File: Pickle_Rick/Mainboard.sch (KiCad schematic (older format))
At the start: 82 parts, among them J10 Conn_01x02_Male, J12 Conn_01x02_Male, J2 8P8C_LED, J3 Micro_SD_Card_Det, J9 Conn_01x02_Male, Q1 MMDT2222A, Q3 PMV20ENR, U1 CP2102N-A01-GQFN24, U2 SN65HVD230, U3 ESP32-WROOM-32D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

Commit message: updated optocoupler, usb kinda weird atm ¯\_(ツ)_/¯
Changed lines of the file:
@@
 $EndComp
 $Sheet
-S 1050 3800 550  800
+S 850  3800 750  750
 U 602F075A
 F0 "usb-c" 50
@@
 F2 "usb_D+" I R 1600 4100 50
 F3 "usb_D-" I R 1600 4250 50
-F4 "usb_ID" I R 1600 4400 50
-F5 "usb_VBUS" I R 1600 3950 50
+F4 "usb_VBUS" I R 1600 3950 50
+F5 "usb_DETONATOR" I R 1600 4400 50
 $EndSheet
 Wire Wire Line

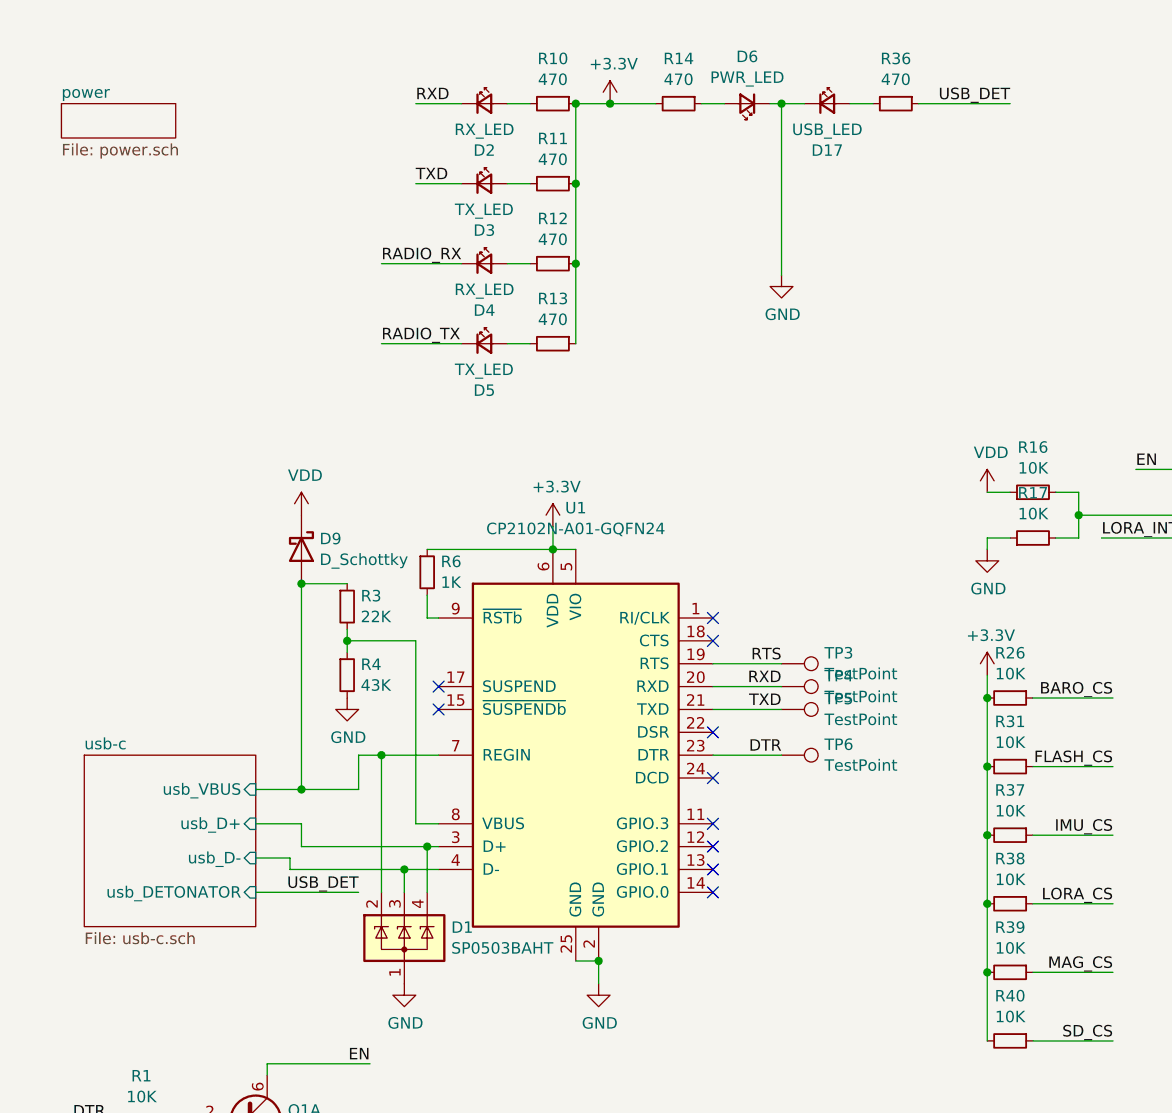
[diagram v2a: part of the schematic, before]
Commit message: fixed led circuit/made sure cc pins are independent
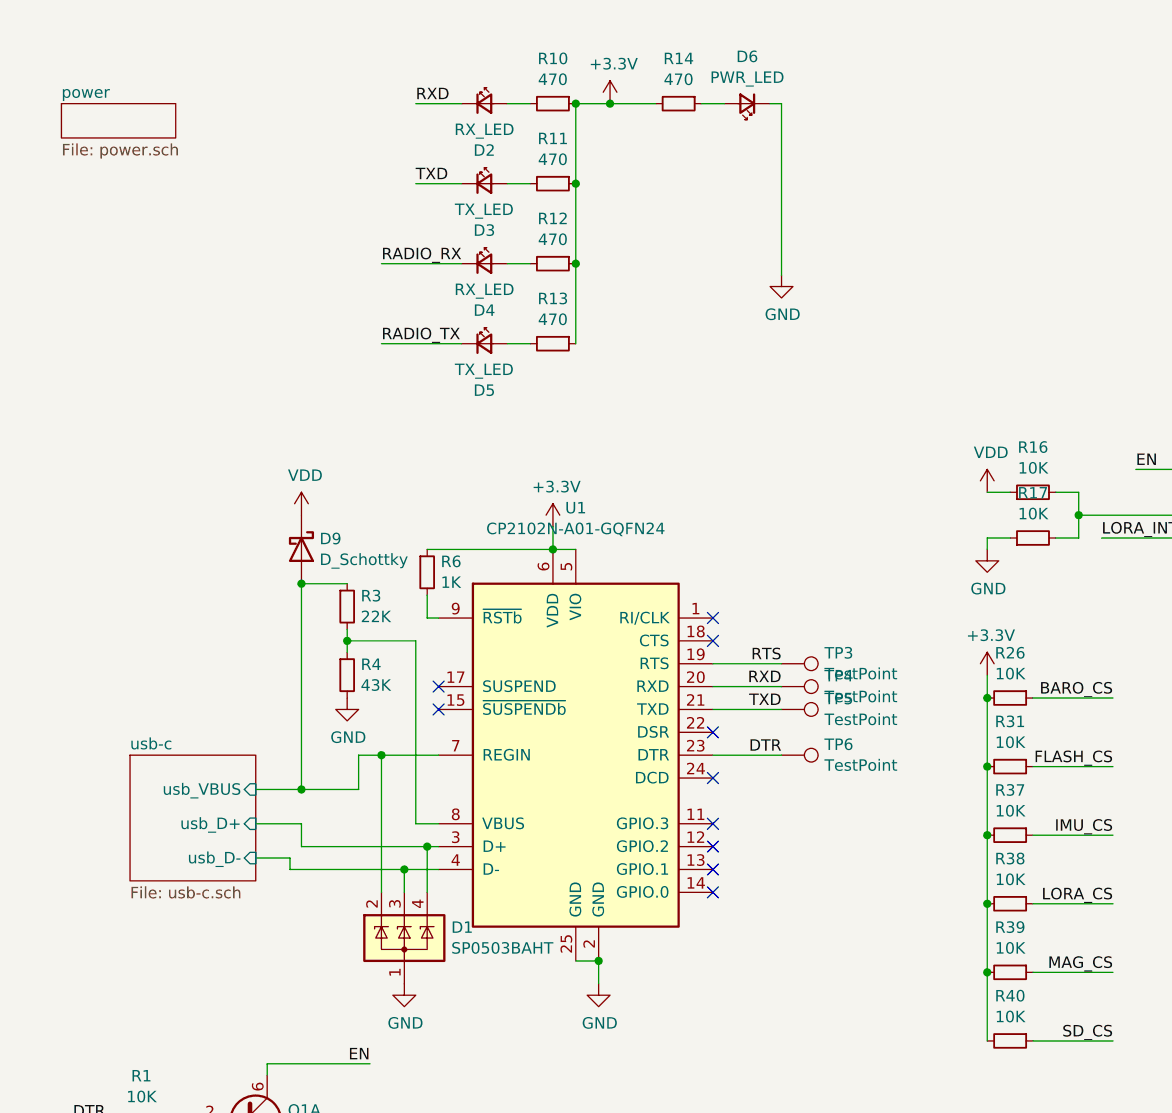
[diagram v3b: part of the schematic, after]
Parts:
- removed D17: USB_LED, LED_SMD:LED_0603_1608Metric_Castellated, symbol Device:LED_Small
- removed R36: 470, Resistor_SMD:R_0603_1608Metric, symbol Device:R_Small
- JP2: footprint iclr-hw:XBEE -> iclr:XBEE
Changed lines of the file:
@@
 SD_CS
-$Comp
-L Sensor_Pressure:MS5607-02BA U5
-U 1 1 5DAF7991
-P 10300 4600
-F 0 "U5" H 10630 4646 50  0000 L CNN
-F 1 "MS5607-02BA" H 10630 4555 50  0000 L CNN
-F 2 "Package_LGA:LGA-8_3x5mm_P1.25mm" H 10300 4600 50  0001 C CNN
-F 3 "https://www.te.com/commerce/DocumentDelivery/DDEController?Action=showdoc&DocId=Data+Sheet%7FMS5607-02BA03%7FB2%7Fpdf%7FEnglish%7FENG_DS_MS5607-02BA03_B2.pdf%7FCAT-BLPS0035" H 10300 4600 50  0001 C CNN
-	1    10300 4600
-	1    0    0    -1
-$EndComp
 $Comp
 L power:+3.3V #PWR034
@@
 F 0 "JP2" H 10350 3910 45  0000 C CNN
 F 1 "XBEE" H 10350 3826 45  0000 C CNN
-F 2 "iclr-hw:XBEE" H 10350 3750 20  0001 C CNN
+F 2 "iclr:XBEE" H 10350 3750 20  0001 C CNN
 F 3 "" H 10350 3150 50  0001 C CNN
 F 4 "XXX-00000" H 10350 3731 60  0000 C CNN "Field4"
@@
 Text Label 2150 2000 0    50   ~ 0
 RADIO_TX
-Text Label 2050 4400 2    50   ~ 0
-USB_DET
-$Comp
-L Device:LED_Small D17
-U 1 1 5DFAB0B1
-P 4100 950
-F 0 "D17" H 4100 745 50  0000 C CNN
-F 1 "USB_LED" H 4100 836 50  0000 C CNN
-F 2 "LED_SMD:LED_0603_1608Metric_Castellated" V 4100 950 50  0001 C CNN
-F 3 "~" V 4100 950 50  0001 C CNN
-	1    4100 950
-	1    0    0    -1
-$EndComp
-$Comp
-L Device:R_Small R36
-U 1 1 5DFAB0B7
-P 4400 950
-F 0 "R36" V 4204 950 50  0000 C CNN
-F 1 "470" V 4295 950 50  0000 C CNN
-F 2 "Resistor_SMD:R_0603_1608Metric" H 4400 950 50  0001 C CNN
-F 3 "~" H 4400 950 50  0001 C CNN
-	1    4400 950
-	0    1    1    0
-$EndComp
-Wire Wire Line
-	4200 950  4300 950
-Wire Wire Line
-	4000 950  3900 950
-Connection ~ 3900 950
-Wire Wire Line
-	4500 950  4900 950
-Text Label 4900 950  2    50   ~ 0
-USB_DET
 $Comp
 L Connector:Conn_01x02_Male J9
@@
 $EndComp
 $Sheet
-S 850  3800 750  750
+S 1050 3800 550  550
 U 602F075A
 F0 "usb-c" 50
@@
 F3 "usb_D-" I R 1600 4250 50
 F4 "usb_VBUS" I R 1600 3950 50
-F5 "usb_DETONATOR" I R 1600 4400 50
 $EndSheet
-Wire Wire Line
-	1600 4400 2050 4400
 Wire Wire Line
 	1800 4200 1800 4100
@@
 	-1   0    0    1
 $EndComp
+$Comp
+L Sensor_Pressure:MS5607-02BA U5
+U 1 1 5DAF7991
+P 10300 4600
+F 0 "U5" H 10630 4646 50  0000 L CNN
+F 1 "MS5607-02BA" H 10630 4555 50  0000 L CNN
+F 2 "Package_LGA:LGA-8_3x5mm_P1.25mm" H 10300 4600 50  0001 C CNN
+F 3 "https://www.te.com/commerce/DocumentDelivery/DDEController?Action=showdoc&DocId=Data+Sheet%7FMS5607-02BA03%7FB2%7Fpdf%7FEnglish%7FENG_DS_MS5607-02BA03_B2.pdf%7FCAT-BLPS0035" H 10300 4600 50  0001 C CNN
+	1    10300 4600
+	1    0    0    -1
+$EndComp
 $EndSCHEMATC

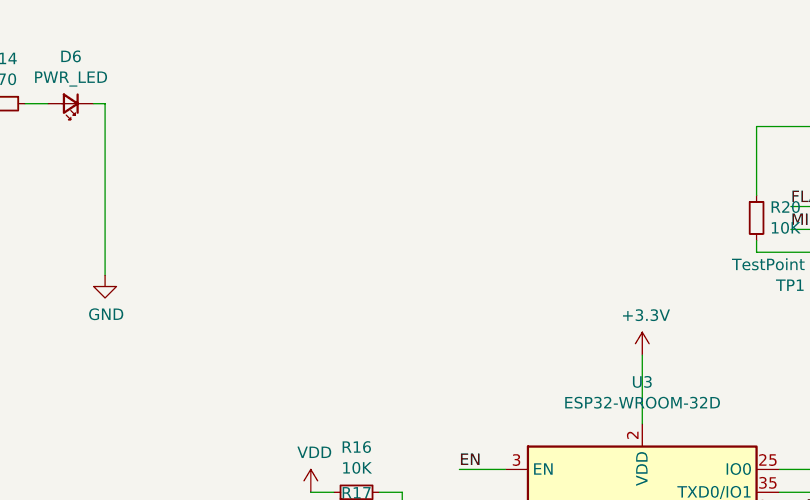
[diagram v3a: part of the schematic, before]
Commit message: might or not have added a rgb port
still need to pick usb footprint; look into smaller buzzer?
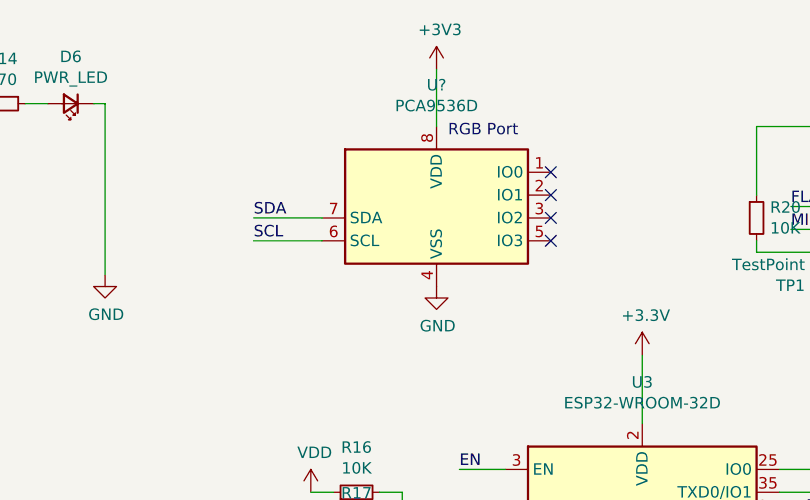
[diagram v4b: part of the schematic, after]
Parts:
- added U?: PCA9536D, Package_SO:SOIC-8_3.9x4.9mm_P1.27mm, symbol Interface_Expansion:PCA9536D
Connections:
- net +3V3: now also U?.8 (VDD)
- net GND: now also U?.4 (VSS)
- net SCL: now also U?.6 (SCL)
- net SDA: now also U?.7 (SDA)
- no-connect marks 40 -> 44
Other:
- note added: "RGB Port"
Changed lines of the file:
@@
 	1    0    0    -1
 $EndComp
+$Comp
+L Interface_Expansion:PCA9536D U?
+U 1 1 60497087
+P 5350 1350
+F 0 "U?" H 5350 1831 50  0000 C CNN
+F 1 "PCA9536D" H 5350 1740 50  0000 C CNN
+F 2 "Package_SO:SOIC-8_3.9x4.9mm_P1.27mm" H 6350 1000 50  0001 C CNN
+F 3 "http://www.nxp.com/documents/data_sheet/PCA9536.pdf" H 5150 -350 50  0001 C CNN
+	1    5350 1350
+	1    0    0    -1
+$EndComp
+$Comp
+L power:+3V3 #PWR?
+U 1 1 604BFA09
+P 5350 800
+F 0 "#PWR?" H 5350 650 50  0001 C CNN
+F 1 "+3V3" H 5365 973 50  0000 C CNN
+F 2 "" H 5350 800 50  0001 C CNN
+F 3 "" H 5350 800 50  0001 C CNN
+	1    5350 800
+	1    0    0    -1
+$EndComp
+$Comp
+L power:GND #PWR?
+U 1 1 604C1D4C
+P 5350 1750
+F 0 "#PWR?" H 5350 1500 50  0001 C CNN
+F 1 "GND" H 5355 1577 50  0000 C CNN
+F 2 "" H 5350 1750 50  0001 C CNN
+F 3 "" H 5350 1750 50  0001 C CNN
+	1    5350 1750
+	1    0    0    -1
+$EndComp
+Wire Wire Line
+	5350 800  5350 1050
+Text Notes 5400 1100 0    50   ~ 0
+RGB Port
+NoConn ~ 5850 1250
+NoConn ~ 5850 1350
+NoConn ~ 5850 1450
+NoConn ~ 5850 1550
+Wire Wire Line
+	4850 1450 4550 1450
+Wire Wire Line
+	4850 1550 4550 1550
+Text Label 4550 1450 0    50   ~ 0
+SDA
+Text Label 4550 1550 0    50   ~ 0
+SCL
 $EndSCHEMATC

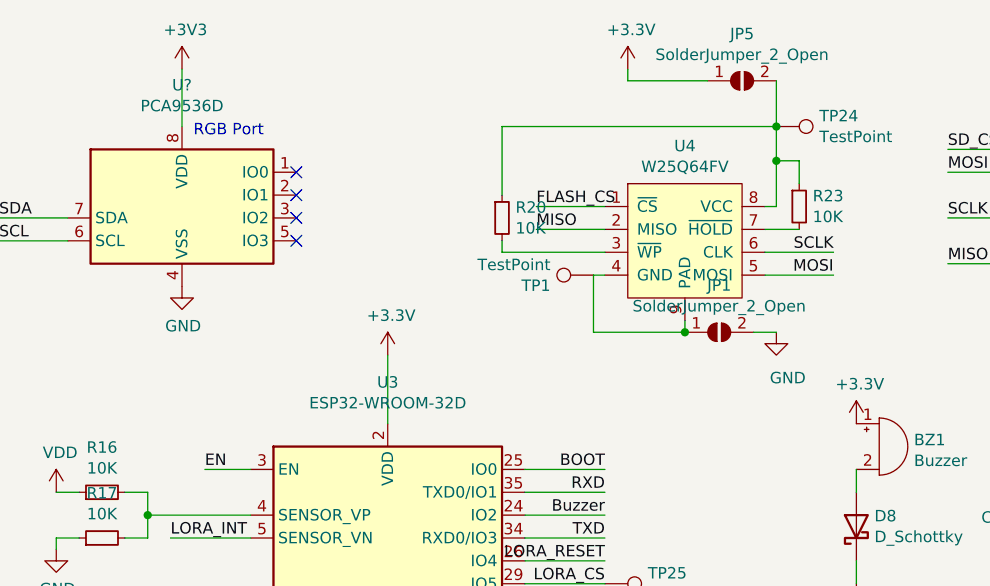
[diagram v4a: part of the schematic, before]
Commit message: changed usb 2.0 to 3.0; started pcb design; changed flash symbol
need to change flash footprint still
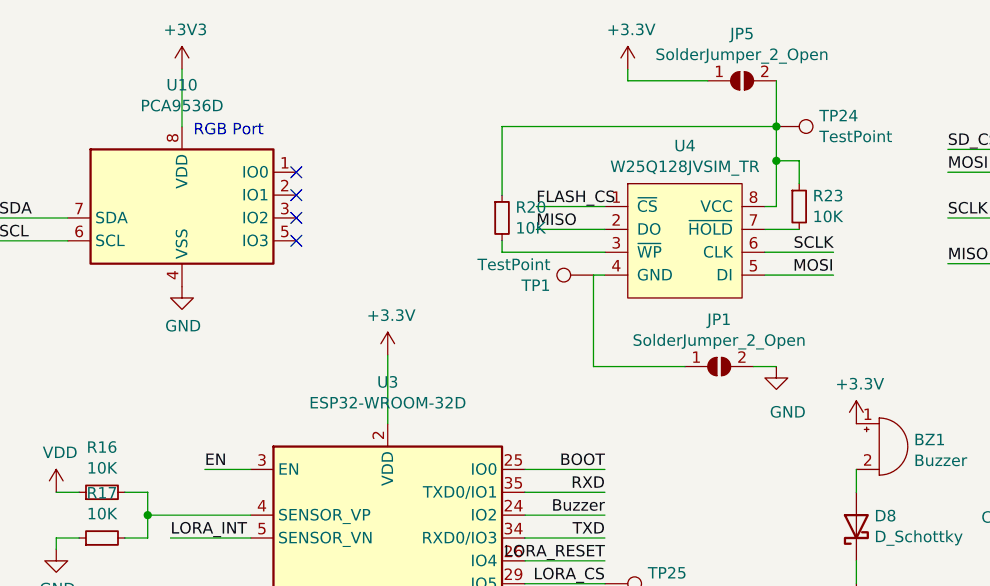
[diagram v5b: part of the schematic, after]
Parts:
- removed U4: W25Q64FV, Package_SO:SOIC-8_3.9x4.9mm_P1.27mm, symbol Mainboard-rescue:W25Q64FV-iclr
- added U4: W25Q128JVSIM_TR, Package_SO:SOIC-8_5.275x5.275mm_P1.27mm, symbol iclr:W25Q128JVSIM_TR
- gave numbers to parts that had none: 1
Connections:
- net FLASH_CS: now also U4.1 (~CS)
- net MISO: now also U4.2 (DO)
- net MOSI: now also U4.5 (DI)
- net SCLK: now also U4.6 (CLK)
- net at JP1.1 (A), TP1.1: now also U4.4 (GND)
- net at JP5.2 (B), R20.1, R23.1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: now also U4.8 (VCC)
- net at R23.2: now also U4.7 (~HOLD)
- net at R20.2: now also U4.3 (~WP)
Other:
- moved on the sheet: JP1

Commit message: did some pcb thing
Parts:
- removed JP2: XBEE, iclr:XBEE, symbol Mainboard-rescue:XBEE-iclr
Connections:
- no-connect marks 44 -> 28
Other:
- moved on the sheet: J12, TP10, TP11, TP14, TP15, TP9, U10

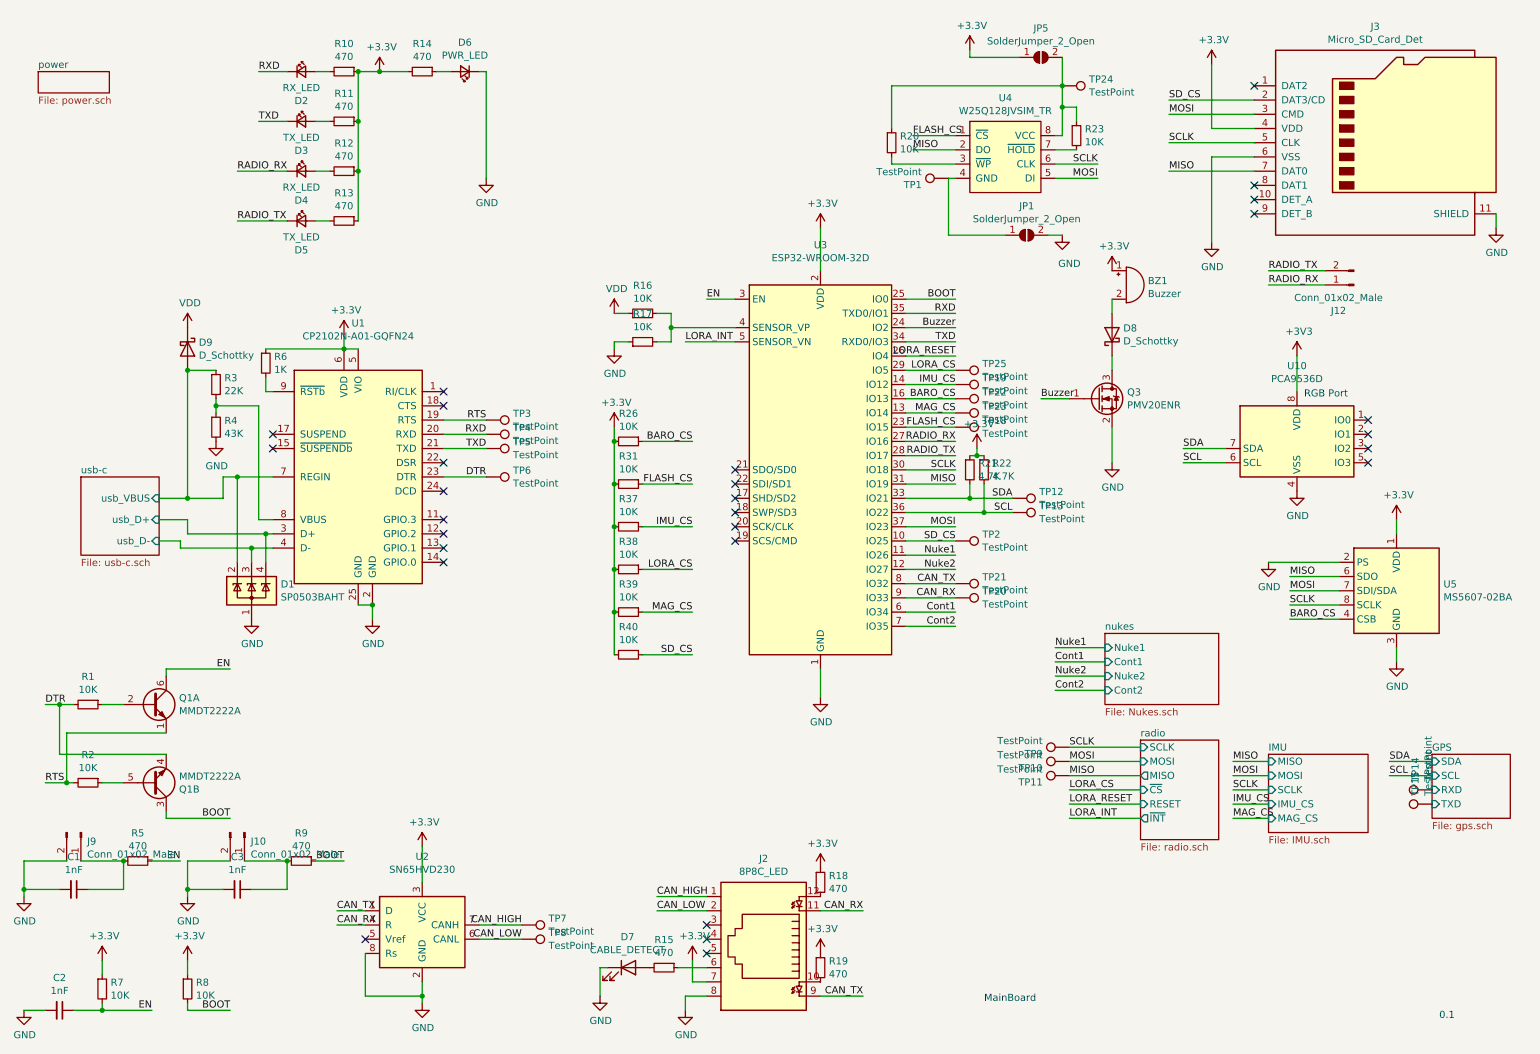
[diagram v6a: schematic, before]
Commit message: not getting farther...
need to double check the buzzer, DS suggests 2 resistors
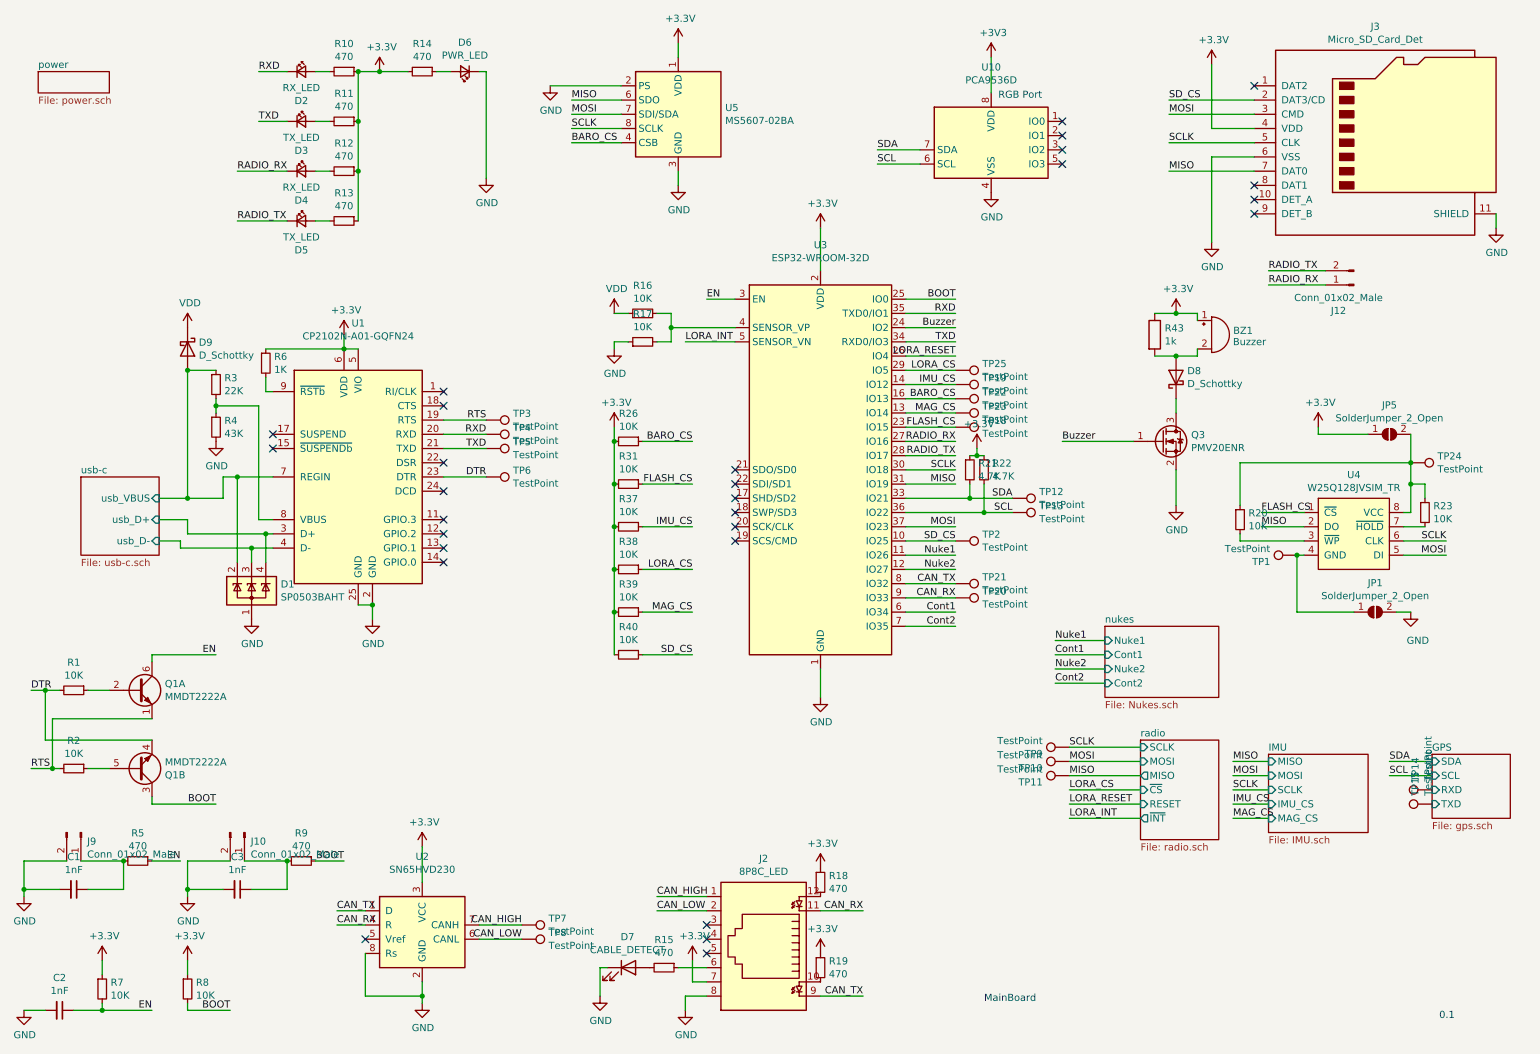
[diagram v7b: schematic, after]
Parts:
- added R43: 1k, Resistor_SMD:R_0603_1608Metric, symbol Device:R
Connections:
- net +3V3: now also R43.1
- net at BZ1.2 (+), D8.2 (A): now also R43.2
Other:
- moved on the sheet: BZ1, D8, JP1, JP5, Q1A, Q1B, Q3, R1, R2, R20, R23, TP1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
